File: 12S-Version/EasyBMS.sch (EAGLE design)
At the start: 148 parts, among them J1 SSM-120-SM-DV, Q10 BSS84LT1G, Q11 BSS84LT1G, Q12 BSS84LT1G, Q13 BSS84LT1G, Q2 BSS84LT1G, Q3 BSS84LT1G, Q4 BSS84LT1G, Q5 BSS84LT1G, Q6 BSS84LT1G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

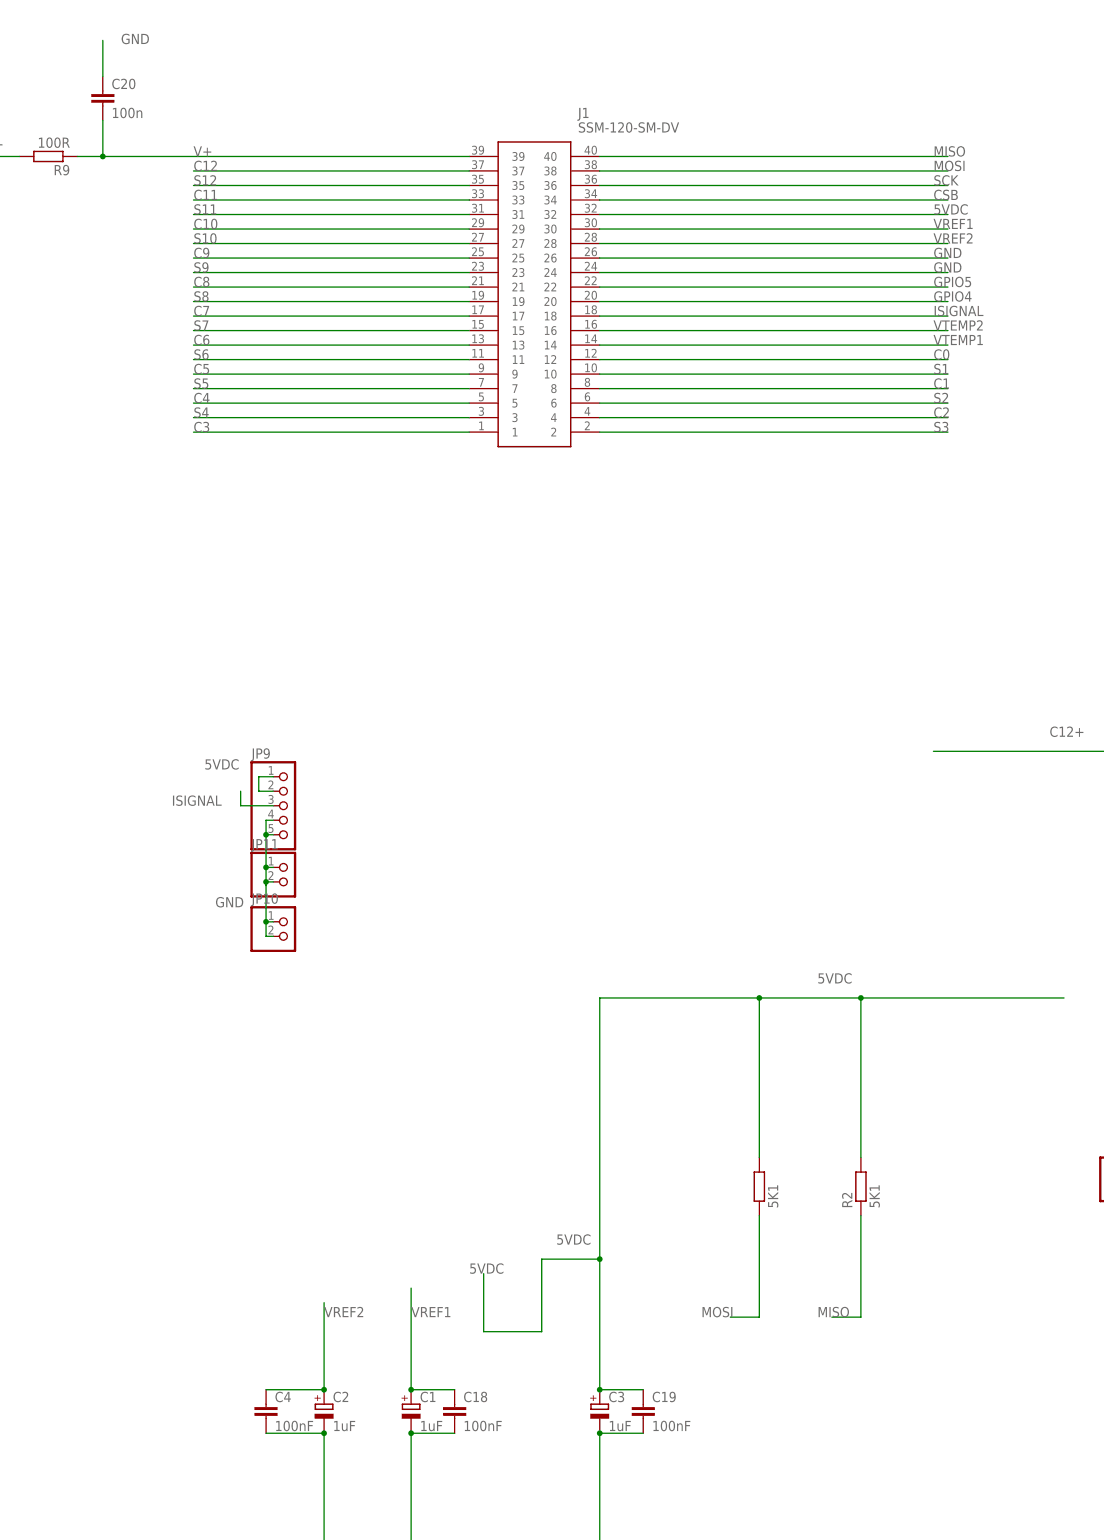
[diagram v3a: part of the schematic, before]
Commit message: IC directly placed on base board, no tracing done
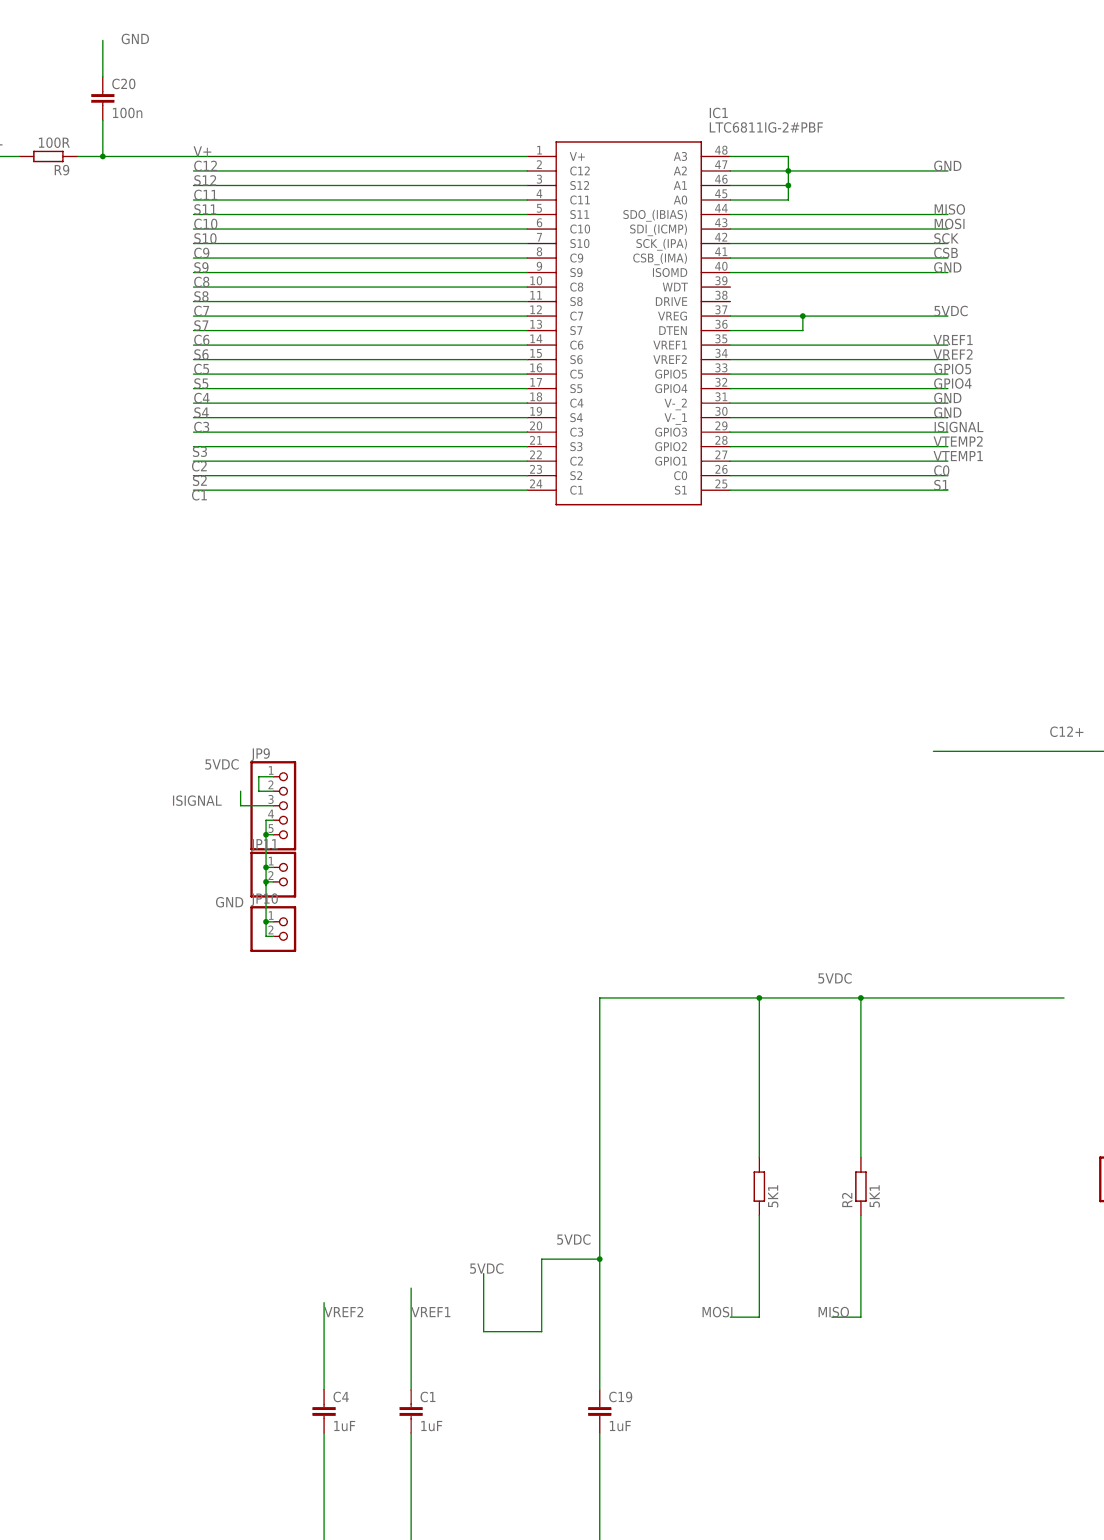
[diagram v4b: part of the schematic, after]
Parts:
- removed C18: 100nF, rcl:C-EUC1206
- removed C2, C3: 1uF, rcl:CPOL-EUE2.5-6
- removed J1: SSM-120-SM-DV, SamacSys_Parts:SSM-120-SM-DV
- added IC1: LTC6811IG-2#PBF, SamacSys_Parts:LTC6811IG-2#PBF
- C1: device rcl:CPOL-EUE2.5-6 -> rcl:C-EUC1206
- C19, C4: value 100nF -> 1uF
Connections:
- net 5VDC: now also IC1.DTEN, IC1.VREG; no longer C3.+, J1.32
- net C0: now also IC1.C0; no longer J1.12
- net C1: now also IC1.C1; no longer J1.8
- net C10: now also IC1.C10; no longer J1.29
- net C11: now also IC1.C11; no longer J1.33
- net C12: now also IC1.C12; no longer J1.37
- net C2: now also IC1.C2; no longer J1.4
- net C3: now also IC1.C3; no longer J1.1
- net C4: now also IC1.C4; no longer J1.5
- net C5: now also IC1.C5; no longer J1.9
- net C6: now also IC1.C6; no longer J1.13
- net C7: now also IC1.C7; no longer J1.17
- net C8: now also IC1.C8; no longer J1.21
- net C9: now also IC1.C9; no longer J1.25
- net CSB: now also IC1.CSB_(IMA); no longer J1.34
- net GND: now also C1.2, IC1.A0, IC1.A1, IC1.A2, IC1.A3, IC1.ISOMD, IC1.V-_1, IC1.V-_2; no longer C1.-, C18.2, C2.-, C3.-, J1.24, J1.26
- net GPIO4: now also IC1.GPIO4; no longer J1.20
- net GPIO5: now also IC1.GPIO5; no longer J1.22
- net ISIGNAL: now also IC1.GPIO3; no longer J1.18
- net MISO: now also IC1.SDO_(IBIAS); no longer J1.40
- net MOSI: now also IC1.SDI_(ICMP); no longer J1.38
- net S1: now also IC1.S1; no longer J1.10
- net S10: now also IC1.S10; no longer J1.27
- net S11: now also IC1.S11; no longer J1.31
- net S12: now also IC1.S12; no longer J1.35
- net S2: now also IC1.S2; no longer J1.6
- net S3: now also IC1.S3; no longer J1.2
- net S4: now also IC1.S4; no longer J1.3
- net S5: now also IC1.S5; no longer J1.7
- net S6: now also IC1.S6; no longer J1.11
- net S7: now also IC1.S7; no longer J1.15
- net S8: now also IC1.S8; no longer J1.19
- net S9: now also IC1.S9; no longer J1.23
- net SCK: now also IC1.SCK_(IPA); no longer J1.36
- net V+: now also IC1.V+; no longer J1.39
- net VREF1: now also C1.1, IC1.VREF1; no longer C1.+, C18.1, J1.30
- net VREF2: now also IC1.VREF2; no longer C2.+, J1.28
- net VTEMP1: now also IC1.GPIO1; no longer J1.14
- net VTEMP2: now also IC1.GPIO2; no longer J1.16
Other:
- moved on the sheet: C19, C4

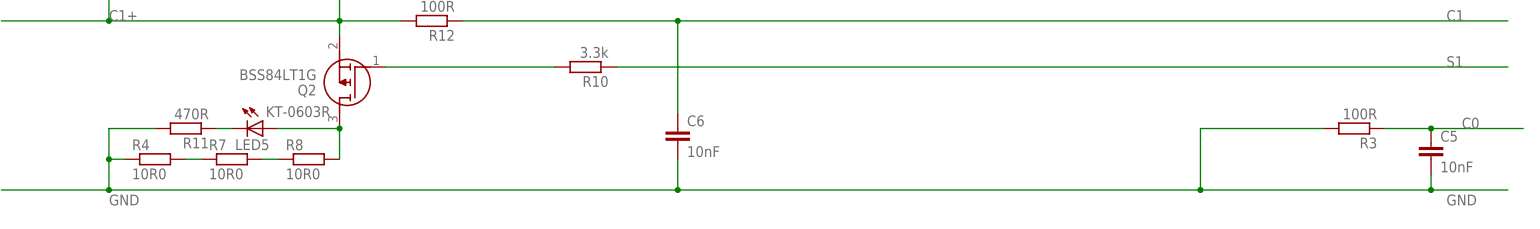
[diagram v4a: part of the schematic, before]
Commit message: Routing nearly done, difficult lines done
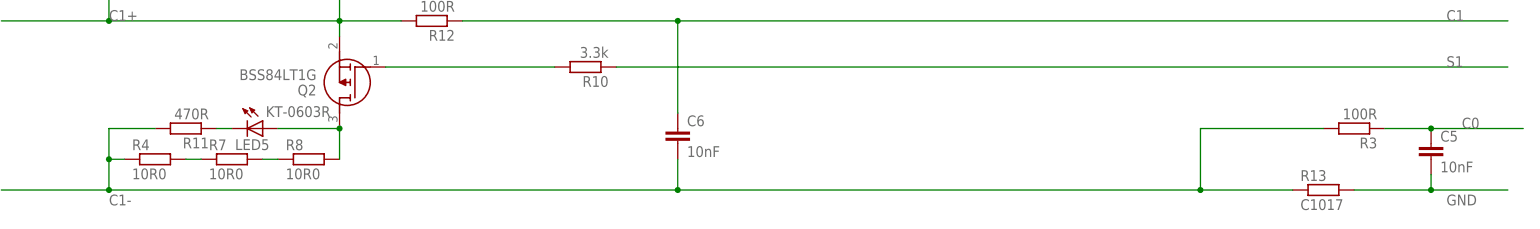
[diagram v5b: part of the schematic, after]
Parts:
- added R13: C1017, rcl:R-EU_R0805
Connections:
- new net C1-: C6.2, R11.2, R13.1, R3.2, R4.1
- net GND: now also R13.2; no longer C6.2, R11.2, R3.2, R4.1
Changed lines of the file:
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@@
 <part name="IC1" library="SamacSys_Parts" deviceset="LTC6811IG-2#PBF" device=""/>
 <part name="C1" library="rcl" library_urn="urn:adsk.eagle:library:334" deviceset="C-EU" device="C1206" package3d_urn="urn:adsk.eagle:package:23618/2" value="1uF"/>
+<part name="R13" library="rcl" library_urn="urn:adsk.eagle:library:334" deviceset="R-EU_" device="R0805" package3d_urn="urn:adsk.eagle:package:23553/2" value="C1017"/>
 </parts>
 <sheets>
@@
 <attribute name="NAME" x="-44.196" y="292.481" size="1.778" layer="95"/>
 <attribute name="VALUE" x="-44.196" y="287.401" size="1.778" layer="96"/>
+</instance>
+<instance part="R13" gate="G$1" x="-200.66" y="66.04" smashed="yes">
+<attribute name="NAME" x="-204.47" y="67.5386" size="1.778" layer="95"/>
+<attribute name="VALUE" x="-204.47" y="62.738" size="1.778" layer="96"/>
 </instance>
 </instances>
@@
 </segment>
 <segment>
-<pinref part="C6" gate="G$1" pin="2"/>
-<wire x1="-307.34" y1="71.12" x2="-307.34" y2="66.04" width="0.1524" layer="91"/>
-<junction x="-307.34" y="66.04"/>
-<wire x1="-307.34" y1="66.04" x2="-220.98" y2="66.04" width="0.1524" layer="91"/>
-<junction x="-401.32" y="71.12"/>
-<pinref part="R4" gate="G$1" pin="1"/>
-<wire x1="-220.98" y1="66.04" x2="-182.88" y2="66.04" width="0.1524" layer="91"/>
-<wire x1="-182.88" y1="66.04" x2="-170.18" y2="66.04" width="0.1524" layer="91"/>
-<wire x1="-398.78" y1="71.12" x2="-401.32" y2="71.12" width="0.1524" layer="91"/>
-<wire x1="-401.32" y1="66.04" x2="-307.34" y2="66.04" width="0.1524" layer="91"/>
-<wire x1="-401.32" y1="71.12" x2="-401.32" y2="66.04" width="0.1524" layer="91"/>
-<pinref part="R11" gate="G$1" pin="2"/>
-<wire x1="-393.7" y1="76.2" x2="-401.32" y2="76.2" width="0.1524" layer="91"/>
-<wire x1="-401.32" y1="76.2" x2="-401.32" y2="71.12" width="0.1524" layer="91"/>
-<label x="-180.34" y="63.5" size="1.778" layer="95"/>
-<label x="-401.32" y="63.5" size="1.778" layer="95"/>
-<junction x="-401.32" y="66.04"/>
-<wire x1="-401.32" y1="66.04" x2="-419.1" y2="66.04" width="0.1524" layer="91"/>
-<pinref part="C5" gate="G$1" pin="2"/>
-<wire x1="-182.88" y1="68.58" x2="-182.88" y2="66.04" width="0.1524" layer="91"/>
-<junction x="-182.88" y="66.04"/>
-<pinref part="R3" gate="G$1" pin="2"/>
-<wire x1="-200.66" y1="76.2" x2="-220.98" y2="76.2" width="0.1524" layer="91"/>
-<wire x1="-220.98" y1="76.2" x2="-220.98" y2="66.04" width="0.1524" layer="91"/>
-<junction x="-220.98" y="66.04"/>
-</segment>
-<segment>
 <pinref part="JP7" gate="G$1" pin="15_TOTAL-"/>
 <wire x1="154.94" y1="497.84" x2="132.08" y2="497.84" width="0.1524" layer="91"/>
@@
 <wire x1="20.32" y1="508" x2="48.26" y2="508" width="0.1524" layer="91"/>
 <label x="45.72" y="508" size="1.778" layer="95"/>
+</segment>
+<segment>
+<pinref part="C5" gate="G$1" pin="2"/>
+<wire x1="-182.88" y1="68.58" x2="-182.88" y2="66.04" width="0.1524" layer="91"/>
+<junction x="-182.88" y="66.04"/>
+<wire x1="-195.58" y1="66.04" x2="-182.88" y2="66.04" width="0.1524" layer="91"/>
+<wire x1="-182.88" y1="66.04" x2="-170.18" y2="66.04" width="0.1524" layer="91"/>
+<label x="-180.34" y="63.5" size="1.778" layer="95"/>
+<pinref part="R13" gate="G$1" pin="2"/>
 </segment>
 </net>
@@
 </segment>
 </net>
+<net name="C1-" class="0">
+<segment>
+<pinref part="C6" gate="G$1" pin="2"/>
+<wire x1="-307.34" y1="71.12" x2="-307.34" y2="66.04" width="0.1524" layer="91"/>
+<junction x="-307.34" y="66.04"/>
+<junction x="-401.32" y="71.12"/>
+<pinref part="R4" gate="G$1" pin="1"/>
+<wire x1="-398.78" y1="71.12" x2="-401.32" y2="71.12" width="0.1524" layer="91"/>
+<wire x1="-401.32" y1="66.04" x2="-307.34" y2="66.04" width="0.1524" layer="91"/>
+<wire x1="-401.32" y1="71.12" x2="-401.32" y2="66.04" width="0.1524" layer="91"/>
+<pinref part="R11" gate="G$1" pin="2"/>
+<wire x1="-393.7" y1="76.2" x2="-401.32" y2="76.2" width="0.1524" layer="91"/>
+<wire x1="-401.32" y1="76.2" x2="-401.32" y2="71.12" width="0.1524" layer="91"/>
+<label x="-401.32" y="63.5" size="1.778" layer="95"/>
+<junction x="-401.32" y="66.04"/>
+<wire x1="-401.32" y1="66.04" x2="-419.1" y2="66.04" width="0.1524" layer="91"/>
+<wire x1="-307.34" y1="66.04" x2="-220.98" y2="66.04" width="0.1524" layer="91"/>
+<pinref part="R3" gate="G$1" pin="2"/>
+<wire x1="-200.66" y1="76.2" x2="-220.98" y2="76.2" width="0.1524" layer="91"/>
+<wire x1="-220.98" y1="76.2" x2="-220.98" y2="66.04" width="0.1524" layer="91"/>
+<junction x="-220.98" y="66.04"/>
+<wire x1="-220.98" y1="66.04" x2="-205.74" y2="66.04" width="0.1524" layer="91"/>
+<pinref part="R13" gate="G$1" pin="1"/>
+</segment>
+</net>

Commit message: cosmetics
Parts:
- removed D2: SM4007PL-TP, SamacSys_Parts:SM4007PL-TP
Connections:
- net 5VDC: no longer D2.A
- net C12+: no longer D2.K
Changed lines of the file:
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@@
 <part name="R3" library="rcl" library_urn="urn:adsk.eagle:library:334" deviceset="R-EU_" device="R0402" package3d_urn="urn:adsk.eagle:package:23547/1" value="100R"/>
 <part name="C5" library="rcl" library_urn="urn:adsk.eagle:library:334" deviceset="C-EU" device="C0402" package3d_urn="urn:adsk.eagle:package:23626/1" value="10nF"/>
-<part name="D2" library="SamacSys_Parts" deviceset="SM4007PL-TP" device=""/>
 <part name="R14" library="rcl" library_urn="urn:adsk.eagle:library:334" deviceset="R-EU_" device="R1206" package3d_urn="urn:adsk.eagle:package:23540/2" value="10R0"/>
 <part name="R20" library="rcl" library_urn="urn:adsk.eagle:library:334" deviceset="R-EU_" device="R1206" package3d_urn="urn:adsk.eagle:package:23540/2" value="10R0"/>
@@
 <attribute name="VALUE" x="-181.356" y="68.961" size="1.778" layer="96"/>
 </instance>
-<instance part="D2" gate="G$1" x="99.06" y="426.72" smashed="yes">
-<attribute name="NAME" x="110.49" y="431.8" size="1.778" layer="95" align="center-left"/>
-<attribute name="VALUE" x="110.49" y="429.26" size="1.778" layer="96" align="center-left"/>
-</instance>
 <instance part="R14" gate="G$1" x="-393.7" y="114.3" smashed="yes">
 <attribute name="NAME" x="-397.51" y="115.7986" size="1.778" layer="95"/>
@@
 <segment>
 <pinref part="U$1" gate="G$1" pin="OUT+"/>
-<wire x1="129.54" y1="406.4" x2="137.16" y2="406.4" width="0.1524" layer="91"/>
-<wire x1="137.16" y1="406.4" x2="195.58" y2="406.4" width="0.1524" layer="91"/>
+<wire x1="129.54" y1="406.4" x2="195.58" y2="406.4" width="0.1524" layer="91"/>
 <wire x1="195.58" y1="406.4" x2="195.58" y2="299.72" width="0.1524" layer="91"/>
-<wire x1="114.3" y1="426.72" x2="137.16" y2="426.72" width="0.1524" layer="91"/>
-<wire x1="137.16" y1="426.72" x2="137.16" y2="406.4" width="0.1524" layer="91"/>
-<junction x="137.16" y="406.4"/>
 <wire x1="195.58" y1="299.72" x2="170.18" y2="299.72" width="0.1524" layer="91"/>
 <label x="177.8" y="297.18" size="1.778" layer="95"/>
@@
 <label x="154.94" y="304.8" size="1.778" layer="95"/>
 <wire x1="170.18" y1="299.72" x2="170.18" y2="302.26" width="0.1524" layer="91"/>
-<pinref part="D2" gate="G$1" pin="A"/>
 </segment>
 <segment>
@@
 <label x="66.04" y="408.94" size="1.778" layer="95"/>
 <pinref part="U$1" gate="G$1" pin="IN+"/>
-<wire x1="93.98" y1="406.4" x2="86.36" y2="406.4" width="0.1524" layer="91"/>
-<wire x1="86.36" y1="406.4" x2="45.72" y2="406.4" width="0.1524" layer="91"/>
-<wire x1="99.06" y1="426.72" x2="86.36" y2="426.72" width="0.1524" layer="91"/>
-<wire x1="86.36" y1="426.72" x2="86.36" y2="406.4" width="0.1524" layer="91"/>
-<junction x="86.36" y="406.4"/>
-<pinref part="D2" gate="G$1" pin="K"/>
-</segment>
-<segment>
+<wire x1="93.98" y1="406.4" x2="45.72" y2="406.4" width="0.1524" layer="91"/>
+</segment>
+<segment>
